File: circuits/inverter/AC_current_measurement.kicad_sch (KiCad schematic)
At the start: 21 parts

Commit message: converts libraries to Kicad 6 format, updates bridge driver
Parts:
- gave numbers to parts that had none: 4
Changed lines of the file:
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@@
   (symbol (lib_id "OSSI_standard_components:Resistor") (at 38.1 41.91 0) (unit 1)
     (in_bom yes) (on_board yes)
-    (property "Reference" "" (id 0) (at 38.1 43.942 0)
+    (property "Reference" "R?" (id 0) (at 38.1 43.942 0)
       (effects (font (size 0.9906 0.9906)))
     )
@@
   (symbol (lib_id "OSSI_standard_components:Capacitor") (at 48.26 48.26 0) (unit 1)
     (in_bom yes) (on_board yes)
-    (property "Reference" "" (id 0) (at 49.784 50.8 0)
+    (property "Reference" "C?" (id 0) (at 49.784 50.8 0)
       (effects (font (size 0.9906 0.9906)) (justify left))
     )
@@
   (symbol (lib_id "OSSI_standard_components:Resistor") (at 66.04 31.75 90) (mirror x) (unit 1)
     (in_bom yes) (on_board yes)
-    (property "Reference" "" (id 0) (at 68.072 31.75 0)
+    (property "Reference" "R?" (id 0) (at 68.072 31.75 0)
       (effects (font (size 0.9906 0.9906)))
     )
@@
   (symbol (lib_id "OSSI_standard_components:Resistor") (at 66.04 68.58 90) (mirror x) (unit 1)
     (in_bom yes) (on_board yes)
-    (property "Reference" "" (id 0) (at 68.072 68.58 0)
+    (property "Reference" "R?" (id 0) (at 68.072 68.58 0)
       (effects (font (size 0.9906 0.9906)))
     )
@@
   (symbol (lib_id "OSSI_standard_components:Resistor") (at 66.04 54.61 90) (mirror x) (unit 1)
     (in_bom yes) (on_board yes)
-    (property "Reference" "" (id 0) (at 68.072 54.61 0)
+    (property "Reference" "R?" (id 0) (at 68.072 54.61 0)
       (effects (font (size 0.9906 0.9906)))
     )
@@
   (symbol (lib_id "OSSI_standard_components:Capacitor") (at 76.2 50.8 0) (unit 1)
     (in_bom yes) (on_board yes)
-    (property "Reference" "" (id 0) (at 77.724 53.34 0)
+    (property "Reference" "C?" (id 0) (at 77.724 53.34 0)
       (effects (font (size 0.9906 0.9906)) (justify left))
     )
@@
   (symbol (lib_id "OSSI_standard_components:Capacitor") (at 97.79 33.02 0) (unit 1)
     (in_bom yes) (on_board yes)
-    (property "Reference" "" (id 0) (at 99.314 35.56 0)
+    (property "Reference" "C?" (id 0) (at 99.314 35.56 0)
       (effects (font (size 0.9906 0.9906)) (justify left))
     )
@@
   (symbol (lib_id "OSSI_standard_components:Resistor") (at 105.41 44.45 0) (unit 1)
     (in_bom yes) (on_board yes)
-    (property "Reference" "" (id 0) (at 105.41 46.482 0)
+    (property "Reference" "R?" (id 0) (at 105.41 46.482 0)
       (effects (font (size 0.9906 0.9906)))
     )
@@
   (symbol (lib_id "OSSI_standard_components:Resistor") (at 115.57 36.83 90) (mirror x) (unit 1)
     (in_bom yes) (on_board yes)
-    (property "Reference" "" (id 0) (at 117.602 36.83 0)
+    (property "Reference" "R?" (id 0) (at 117.602 36.83 0)
       (effects (font (size 0.9906 0.9906)))
     )
@@
   (symbol (lib_id "OSSI_standard_components:PNP") (at 125.73 31.75 90) (unit 1)
     (in_bom yes) (on_board yes)
-    (property "Reference" "" (id 0) (at 128.27 35.56 90)
+    (property "Reference" "Q?" (id 0) (at 128.27 35.56 90)
       (effects (font (size 0.9906 0.9906)) (justify right))
     )
@@
   (symbol (lib_id "OSSI_standard_components:DUAL_OPAMP") (at 88.9 44.45 0) (unit 1)
     (in_bom yes) (on_board yes)
-    (property "Reference" "" (id 0) (at 87.63 50.673 0)
+    (property "Reference" "U?" (id 0) (at 87.63 50.673 0)
       (effects (font (size 0.9906 0.9906)) (justify right))
     )
@@
   (symbol (lib_id "acs722:ACS722") (at 88.9 104.14 0) (unit 1)
     (in_bom yes) (on_board yes)
-    (property "Reference" "" (id 0) (at 88.9 113.03 0)
+    (property "Reference" "U?" (id 0) (at 88.9 113.03 0)
       (effects (font (size 0.9906 0.9906)))
     )
@@
   (symbol (lib_id "OSSI_standard_components:Capacitor") (at 67.31 110.49 0) (unit 1)
     (in_bom yes) (on_board yes)
-    (property "Reference" "" (id 0) (at 68.834 113.03 0)
+    (property "Reference" "C?" (id 0) (at 68.834 113.03 0)
       (effects (font (size 0.9906 0.9906)) (justify left))
     )
@@
   (symbol (lib_id "OSSI_standard_components:Resistor") (at 96.52 116.84 0) (unit 1)
     (in_bom yes) (on_board yes)
-    (property "Reference" "" (id 0) (at 96.52 118.872 0)
+    (property "Reference" "R?" (id 0) (at 96.52 118.872 0)
       (effects (font (size 0.9906 0.9906)))
     )
@@
   (symbol (lib_id "OSSI_standard_components:Capacitor") (at 129.54 111.76 0) (unit 1)
     (in_bom yes) (on_board yes)
-    (property "Reference" "" (id 0) (at 131.064 114.3 0)
+    (property "Reference" "C?" (id 0) (at 131.064 114.3 0)
       (effects (font (size 0.9906 0.9906)) (justify left))
     )
@@
   (symbol (lib_id "OSSI_standard_components:DUAL_OPAMP") (at 213.36 119.38 0) (unit 2)
     (in_bom yes) (on_board yes)
-    (property "Reference" "" (id 0) (at 212.09 125.603 0)
+    (property "Reference" "U?" (id 0) (at 212.09 125.603 0)
       (effects (font (size 0.9906 0.9906)) (justify right))
     )
@@
   (symbol (lib_id "OSSI_standard_components:Resistor") (at 233.68 119.38 0) (unit 1)
     (in_bom yes) (on_board yes)
-    (property "Reference" "" (id 0) (at 233.68 121.412 0)
+    (property "Reference" "R?" (id 0) (at 233.68 121.412 0)
       (effects (font (size 0.9906 0.9906)))
     )
@@
   (symbol (lib_id "OSSI_standard_components:Capacitor") (at 207.01 137.16 0) (unit 1)
     (in_bom yes) (on_board yes)
-    (property "Reference" "" (id 0) (at 208.534 139.7 0)
+    (property "Reference" "C?" (id 0) (at 208.534 139.7 0)
       (effects (font (size 0.9906 0.9906)) (justify left))
     )
@@
   (symbol (lib_id "OSSI_standard_components:Resistor") (at 198.12 114.3 90) (mirror x) (unit 1)
     (in_bom yes) (on_board yes)
-    (property "Reference" "" (id 0) (at 200.152 114.3 0)
+    (property "Reference" "R?" (id 0) (at 200.152 114.3 0)
       (effects (font (size 0.9906 0.9906)))
     )
@@
   (symbol (lib_id "OSSI_standard_components:Resistor") (at 198.12 130.81 90) (mirror x) (unit 1)
     (in_bom yes) (on_board yes)
-    (property "Reference" "" (id 0) (at 200.152 130.81 0)
+    (property "Reference" "R?" (id 0) (at 200.152 130.81 0)
       (effects (font (size 0.9906 0.9906)))
     )
@@
   (symbol (lib_id "OSSI_standard_components:Resistor") (at 198.12 144.78 90) (mirror x) (unit 1)
     (in_bom yes) (on_board yes)
-    (property "Reference" "" (id 0) (at 200.152 144.78 0)
-      (effects (font (size 0.9906 0.9906)))
-    )
+    (property "Reference" "R?" (id 0) (at 200.152 144.78 0)
+      (effects (font (size 0.9906 0.9906)))
+    )

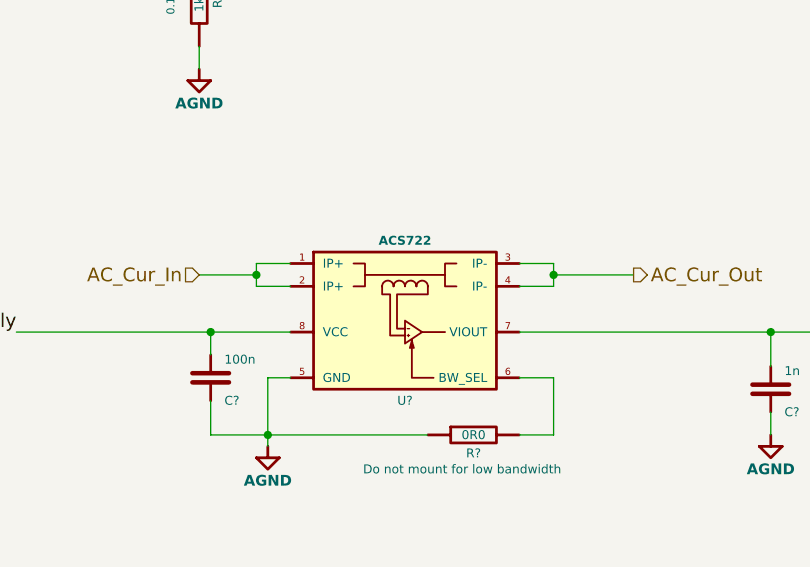
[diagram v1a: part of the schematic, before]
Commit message: converts the project to Kicad 7
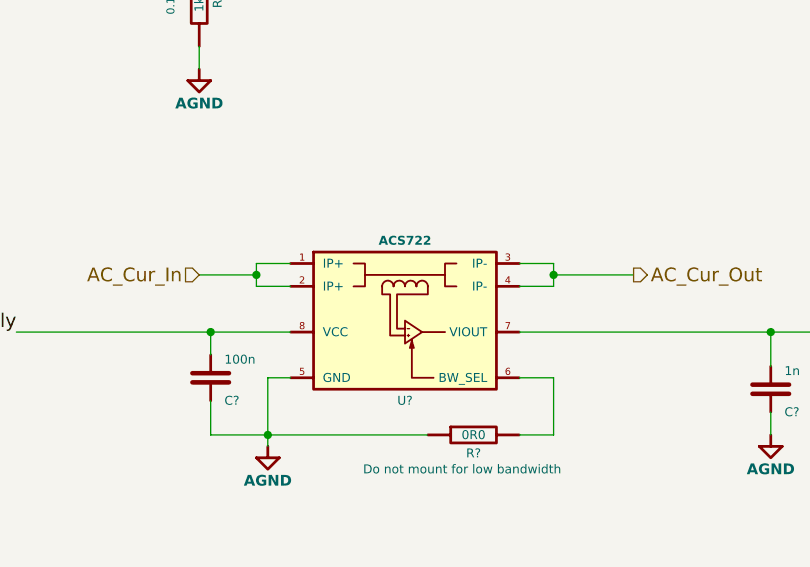
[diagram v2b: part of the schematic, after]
